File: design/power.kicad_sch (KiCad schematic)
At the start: 56 parts, among them J1 POWER, U1 LM3880MF-1AA, U2 NCP59744MN1, U3 NCP59744MN1, U4 NCP59744MN1, U5 NCP59744MN1

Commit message: Updated schematic
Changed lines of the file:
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@@
   (junction (at 242.57 123.19))
   (junction (at 251.46 29.21))
+  (no_connect (at 85.09 87.63))
+  (no_connect (at 199.39 86.36))
   (no_connect (at 199.39 135.89))
-  (no_connect (at 199.39 86.36))
   (no_connect (at 85.09 135.89))
-  (no_connect (at 85.09 87.63))
   (wire (pts (xy 39.37 161.29) (xy 39.37 163.83)))
   (wire (pts (xy 39.37 171.45) (xy 39.37 175.26)))
@@
   (wire (pts (xy 251.46 29.21) (xy 252.73 29.21)))
   (wire (pts (xy 251.46 38.1) (xy 251.46 39.37)))
+  (polyline (pts (xy 120.65 172.72) (xy 127 172.72)))
+  (polyline (pts (xy 120.65 175.26) (xy 129.54 175.26)))
+  (polyline (pts (xy 120.65 177.8) (xy 132.08 177.8)))
+  (polyline (pts (xy 127 168.91) (xy 151.13 168.91)))
+  (polyline (pts (xy 127 172.72) (xy 127 168.91)))
+  (polyline (pts (xy 129.54 171.45) (xy 148.59 171.45)))
+  (polyline (pts (xy 129.54 175.26) (xy 129.54 171.45)))
+  (polyline (pts (xy 132.08 173.99) (xy 146.05 173.99)))
+  (polyline (pts (xy 132.08 177.8) (xy 132.08 173.99)))
+  (polyline (pts (xy 146.05 173.99) (xy 146.05 177.8)))
+  (polyline (pts (xy 146.05 177.8) (xy 161.29 177.8)))
+  (polyline (pts (xy 148.59 171.45) (xy 148.59 175.26)))
+  (polyline (pts (xy 148.59 175.26) (xy 161.29 175.26)))
+  (polyline (pts (xy 151.13 168.91) (xy 151.13 172.72)))
+  (polyline (pts (xy 151.13 172.72) (xy 161.29 172.72)))
   (text "Práh 1V25\nSpínáno při 4V45" (at 35.56 181.61 180)
     (effects (font (size 1.27 1.27)) (justify right bottom))

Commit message: Updated notes
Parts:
- renumbered C24 to C?, C14 to C?, C19 to C?, C2 to C?, C11 to C?, C4 to C?, C1 to C?, C12 to C?, C15 to C?, C25 to C?, C3 to C?, C16 to C?, C20 to C?, C23 to C?, C29 to C?, C7 to C?, C10 to C?, C17 to C?, C5 to C?, C28 to C?, C27 to C?, C13 to C?, C6 to C?, C18 to C?, C21 to C?, C9 to C?, C26 to C?, C8 to C?, C22 to C?, D1 to D?, D2 to D?, D3 to D?, D6 to D?, D5 to D?, D4 to D?, FB1 to FB?, J1 to J?, L1 to L?, R10 to R?, R9 to R?, R13 to R?, R12 to R?, R7 to R?, R6 to R?, R1 to R?, R3 to R?, R11 to R?, R8 to R?, R4 to R?, R5 to R?, R2 to R?, U3 to U?, U4 to U?, U2 to U?, U1 to U?, U5 to U?

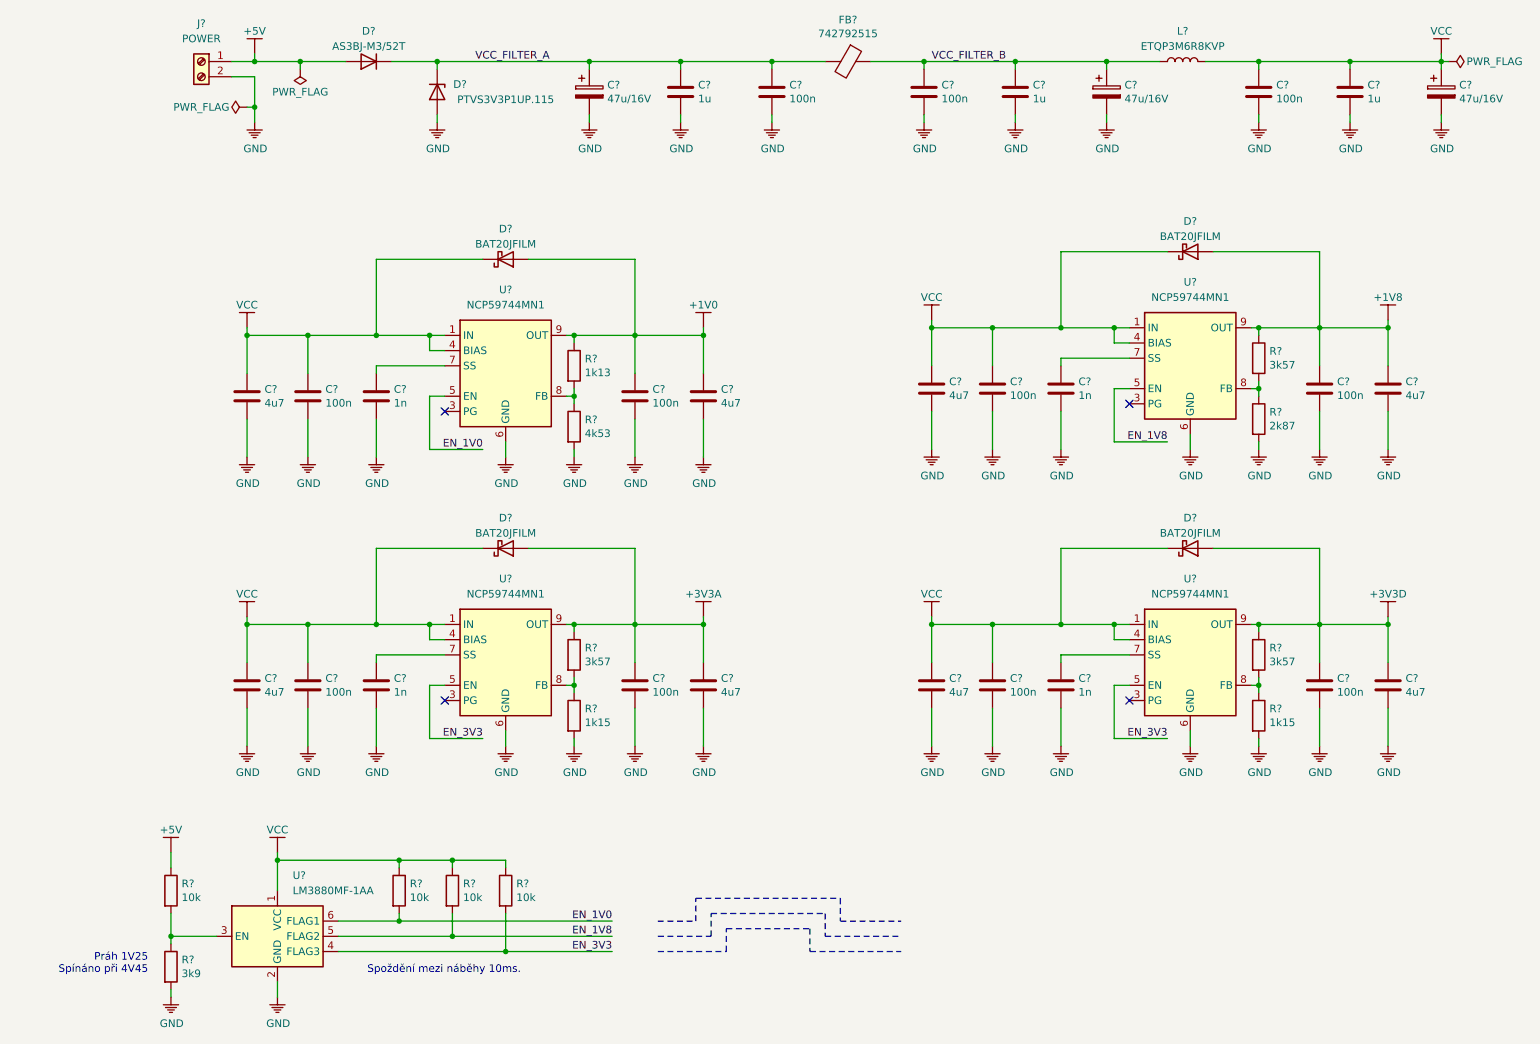
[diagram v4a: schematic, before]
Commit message: Fixed ADC PWRDN problem
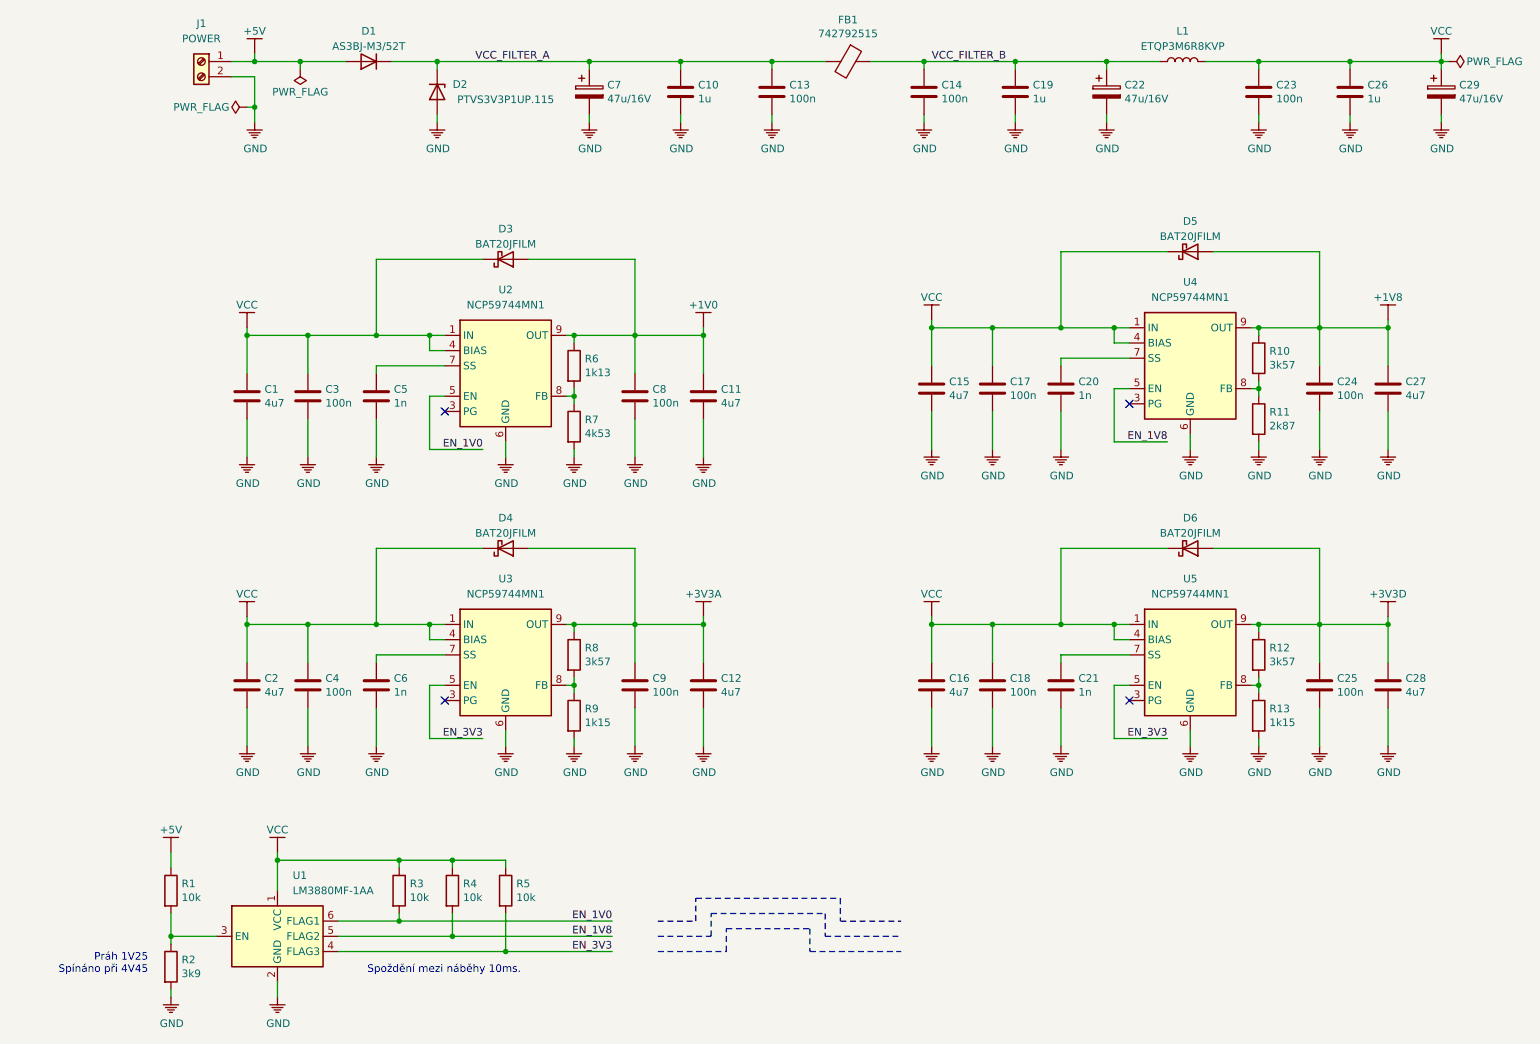
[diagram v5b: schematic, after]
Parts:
- gave numbers to parts that had none: 56

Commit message: Added net classes
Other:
- title: Digitizer 10b 105 MSPS with FPGA -> Digitizer 10b 100 MSPS with FPGA
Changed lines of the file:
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@@
-(kicad_sch (version 20200618) (host eeschema "5.99.0-unknown-f420396~101~ubuntu18.04.1")
+(kicad_sch (version 20200714) (host eeschema "5.99.0-unknown-039b6fd~102~ubuntu18.04.1")
   (page 1 8)
   (paper "A4")
   (title_block
-    (title "Digitizer 10b 105 MSPS with FPGA")
+    (title "Digitizer 10b 100 MSPS with FPGA")
     (date "2020-03-09")
     (rev "1.0")
@@
   )
   (junction (at 39.37 175.26) (diameter 0) (color 0 0 0 0))
-  (junction (at 52.07 74.93) (diameter 0) (color 0 0 0 0))
-  (junction (at 52.07 123.19) (diameter 0) (color 0 0 0 0))
-  (junction (at 53.34 29.21) (diameter 0) (color 0 0 0 0))
-  (junction (at 53.34 36.83) (diameter 0) (color 0 0 0 0))
-  (junction (at 57.15 162.56) (diameter 0) (color 0 0 0 0))
-  (junction (at 60.96 29.21) (diameter 0) (color 0 0 0 0))
-  (junction (at 62.23 74.93) (diameter 0) (color 0 0 0 0))
-  (junction (at 62.23 123.19) (diameter 0) (color 0 0 0 0))
-  (junction (at 73.66 74.93) (diameter 0) (color 0 0 0 0))
-  (junction (at 73.66 123.19) (diameter 0) (color 0 0 0 0))
-  (junction (at 77.47 162.56) (diameter 0) (color 0 0 0 0))
+  (junction (at 52.07 74.93) (diameter 0) (color 255 0 0 1))
+  (junction (at 52.07 123.19) (diameter 0) (color 255 0 0 1))
+  (junction (at 53.34 29.21) (diameter 0) (color 255 0 0 1))
+  (junction (at 53.34 36.83) (diameter 0) (color 0 0 255 1))
+  (junction (at 57.15 162.56) (diameter 0) (color 255 0 0 1))
+  (junction (at 60.96 29.21) (diameter 0) (color 255 0 0 1))
+  (junction (at 62.23 74.93) (diameter 0) (color 255 0 0 1))
+  (junction (at 62.23 123.19) (diameter 0) (color 255 0 0 1))
+  (junction (at 73.66 74.93) (diameter 0) (color 255 0 0 1))
+  (junction (at 73.66 123.19) (diameter 0) (color 255 0 0 1))
+  (junction (at 77.47 162.56) (diameter 0) (color 255 0 0 1))
   (junction (at 77.47 172.72) (diameter 0) (color 0 0 0 0))
-  (junction (at 82.55 74.93) (diameter 0) (color 0 0 0 0))
-  (junction (at 82.55 123.19) (diameter 0) (color 0 0 0 0))
-  (junction (at 83.82 29.21) (diameter 0) (color 0 0 0 0))
-  (junction (at 86.36 162.56) (diameter 0) (color 0 0 0 0))
+  (junction (at 82.55 74.93) (diameter 0) (color 255 0 0 1))
+  (junction (at 82.55 123.19) (diameter 0) (color 255 0 0 1))
+  (junction (at 83.82 29.21) (diameter 0) (color 255 0 0 1))
+  (junction (at 86.36 162.56) (diameter 0) (color 255 0 0 1))
   (junction (at 86.36 175.26) (diameter 0) (color 0 0 0 0))
   (junction (at 95.25 177.8) (diameter 0) (color 0 0 0 0))
-  (junction (at 106.68 74.93) (diameter 0) (color 0 0 0 0))
+  (junction (at 106.68 74.93) (diameter 0) (color 255 0 0 1))
   (junction (at 106.68 85.09) (diameter 0) (color 0 0 0 0))
-  (junction (at 106.68 123.19) (diameter 0) (color 0 0 0 0))
+  (junction (at 106.68 123.19) (diameter 0) (color 255 0 0 1))
   (junction (at 106.68 133.35) (diameter 0) (color 0 0 0 0))
-  (junction (at 109.22 29.21) (diameter 0) (color 0 0 0 0))
-  (junction (at 116.84 74.93) (diameter 0) (color 0 0 0 0))
-  (junction (at 116.84 123.19) (diameter 0) (color 0 0 0 0))
-  (junction (at 124.46 29.21) (diameter 0) (color 0 0 0 0))
-  (junction (at 128.27 74.93) (diameter 0) (color 0 0 0 0))
-  (junction (at 128.27 123.19) (diameter 0) (color 0 0 0 0))
-  (junction (at 139.7 29.21) (diameter 0) (color 0 0 0 0))
-  (junction (at 165.1 29.21) (diameter 0) (color 0 0 0 0))
-  (junction (at 166.37 73.66) (diameter 0) (color 0 0 0 0))
-  (junction (at 166.37 123.19) (diameter 0) (color 0 0 0 0))
-  (junction (at 176.53 73.66) (diameter 0) (color 0 0 0 0))
-  (junction (at 176.53 123.19) (diameter 0) (color 0 0 0 0))
-  (junction (at 180.34 29.21) (diameter 0) (color 0 0 0 0))
-  (junction (at 187.96 73.66) (diameter 0) (color 0 0 0 0))
-  (junction (at 187.96 123.19) (diameter 0) (color 0 0 0 0))
-  (junction (at 195.58 29.21) (diameter 0) (color 0 0 0 0))
-  (junction (at 196.85 73.66) (diameter 0) (color 0 0 0 0))
-  (junction (at 196.85 123.19) (diameter 0) (color 0 0 0 0))
-  (junction (at 220.98 29.21) (diameter 0) (color 0 0 0 0))
-  (junction (at 220.98 73.66) (diameter 0) (color 0 0 0 0))
+  (junction (at 109.22 29.21) (diameter 0) (color 255 0 0 1))
+  (junction (at 116.84 74.93) (diameter 0) (color 255 0 0 1))
+  (junction (at 116.84 123.19) (diameter 0) (color 255 0 0 1))
+  (junction (at 124.46 29.21) (diameter 0) (color 255 0 0 1))
+  (junction (at 128.27 74.93) (diameter 0) (color 255 0 0 1))
+  (junction (at 128.27 123.19) (diameter 0) (color 255 0 0 1))
+  (junction (at 139.7 29.21) (diameter 0) (color 255 0 0 1))
+  (junction (at 165.1 29.21) (diameter 0) (color 255 0 0 1))
+  (junction (at 166.37 73.66) (diameter 0) (color 255 0 0 1))
+  (junction (at 166.37 123.19) (diameter 0) (color 255 0 0 1))
+  (junction (at 176.53 73.66) (diameter 0) (color 255 0 0 1))
+  (junction (at 176.53 123.19) (diameter 0) (color 255 0 0 1))
+  (junction (at 180.34 29.21) (diameter 0) (color 255 0 0 1))
+  (junction (at 187.96 73.66) (diameter 0) (color 255 0 0 1))
+  (junction (at 187.96 123.19) (diameter 0) (color 255 0 0 1))
+  (junction (at 195.58 29.21) (diameter 0) (color 255 0 0 1))
+  (junction (at 196.85 73.66) (diameter 0) (color 255 0 0 1))
+  (junction (at 196.85 123.19) (diameter 0) (color 255 0 0 1))
+  (junction (at 220.98 29.21) (diameter 0) (color 255 0 0 1))
+  (junction (at 220.98 73.66) (diameter 0) (color 255 0 0 1))
   (junction (at 220.98 83.82) (diameter 0) (color 0 0 0 0))
-  (junction (at 220.98 123.19) (diameter 0) (color 0 0 0 0))
+  (junction (at 220.98 123.19) (diameter 0) (color 255 0 0 1))
   (junction (at 220.98 133.35) (diameter 0) (color 0 0 0 0))
-  (junction (at 231.14 73.66) (diameter 0) (color 0 0 0 0))
-  (junction (at 231.14 123.19) (diameter 0) (color 0 0 0 0))
-  (junction (at 236.22 29.21) (diameter 0) (color 0 0 0 0))
-  (junction (at 242.57 73.66) (diameter 0) (color 0 0 0 0))
-  (junction (at 242.57 123.19) (diameter 0) (color 0 0 0 0))
-  (junction (at 251.46 29.21) (diameter 0) (color 0 0 0 0))
-  (no_connect (at 199.39 135.89))
+  (junction (at 231.14 73.66) (diameter 0) (color 255 0 0 1))
+  (junction (at 231.14 123.19) (diameter 0) (color 255 0 0 1))
+  (junction (at 236.22 29.21) (diameter 0) (color 255 0 0 1))
+  (junction (at 242.57 73.66) (diameter 0) (color 255 0 0 1))
+  (junction (at 242.57 123.19) (diameter 0) (color 255 0 0 1))
+  (junction (at 251.46 29.21) (diameter 0) (color 255 0 0 1))
+  (no_connect (at 85.09 87.63))
   (no_connect (at 85.09 135.89))
   (no_connect (at 199.39 86.36))
-  (no_connect (at 85.09 87.63))
+  (no_connect (at 199.39 135.89))
   (wire (pts (xy 39.37 161.29) (xy 39.37 163.83))
     (stroke (width 0) (type solid) (color 0 0 0 0))
